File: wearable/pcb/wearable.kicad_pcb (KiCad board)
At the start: 4 copper layers, 28 x 39.2 mm, 83 parts, among them J1 USB_C_Receptacle_USB2.0, J2 Extension, J3 Extension, U1 BC833, U10 TCR3UFxxA, U11 TMP1075, U2 MCP73832-2-OT, U3 S-85S1A, U4 LIS2DE12, U5 APDS-9250, U6 MX25R8035FZxxx0, U7 PCF85063ATL, U8 DT1446-04V, U9 MAX30102, Y71 32.768kHz

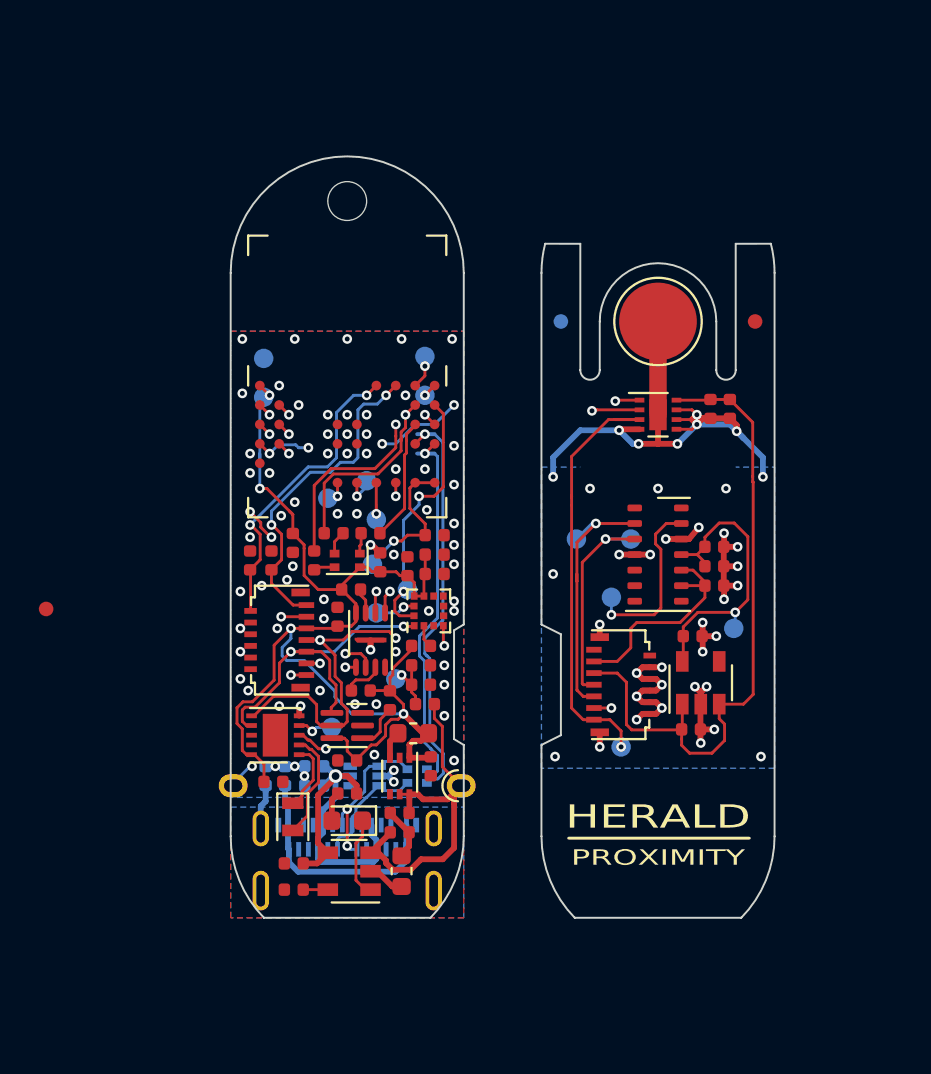
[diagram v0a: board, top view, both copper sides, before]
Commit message: The very first prototype, panelized.
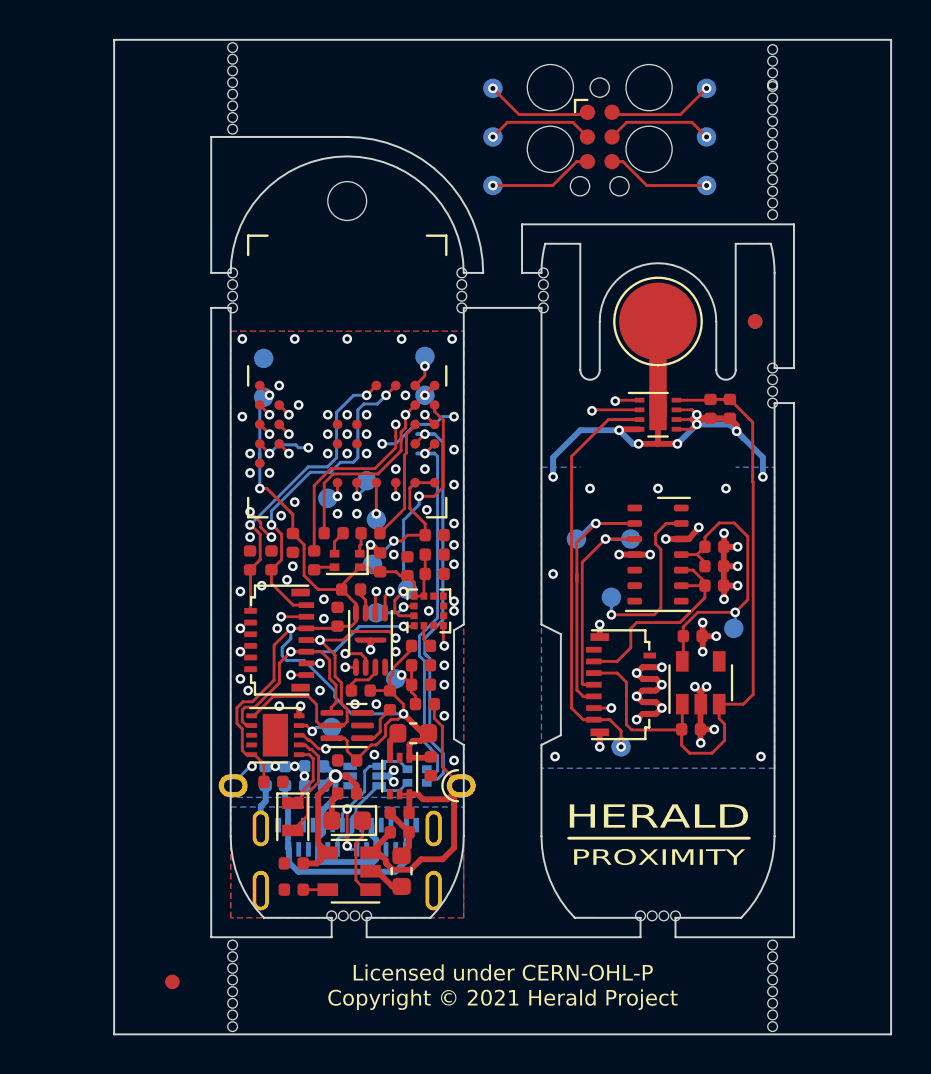
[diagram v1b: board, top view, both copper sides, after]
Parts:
- added J4: TagConnect, Connector:Tag-Connect_TC2030-IDC-FP_2x03_P1.27mm_Vertical, F.Cu at (163.0, 78.5)
- added REF**: MouseBites_4x0.5mm, Herald_Extras:MouseBites_4x0.5mm, F.Cu at (171.9, 74.9)
- added REF**: MouseBites_4x0.5mm, Herald_Extras:MouseBites_4x0.5mm, F.Cu at (166.0, 118.6)
- added REF**: MouseBites_4x0.5mm, Herald_Extras:MouseBites_4x0.5mm, F.Cu at (150.1, 118.6)
- added REF**: MouseBites_4x0.5mm, Herald_Extras:MouseBites_4x0.5mm, F.Cu at (144.1, 77.2)
- added REF**: MouseBites_4x0.5mm, Herald_Extras:MouseBites_4x0.5mm, F.Cu at (171.9, 121.0)
- added REF**: MouseBites_4x0.5mm, Herald_Extras:MouseBites_4x0.5mm, F.Cu at (171.9, 91.3)
- added REF**: MouseBites_4x0.5mm, Herald_Extras:MouseBites_4x0.5mm, F.Cu at (160.1, 86.4)
- added REF**: MouseBites_4x0.5mm, Herald_Extras:MouseBites_4x0.5mm, F.Cu at (155.9, 86.4)
- added REF**: MouseBites_4x0.5mm, Herald_Extras:MouseBites_4x0.5mm, F.Cu at (171.9, 76.8)
- added REF**: MouseBites_4x0.5mm, Herald_Extras:MouseBites_4x0.5mm, F.Cu at (171.9, 79.2)
- added REF**: MouseBites_4x0.5mm, Herald_Extras:MouseBites_4x0.5mm, F.Cu at (171.9, 81.6)
- added REF**: MouseBites_4x0.5mm, Herald_Extras:MouseBites_4x0.5mm, F.Cu at (171.9, 123.4)
- added REF**: MouseBites_4x0.5mm, Herald_Extras:MouseBites_4x0.5mm, F.Cu at (144.1, 123.4)
- added REF**: MouseBites_4x0.5mm, Herald_Extras:MouseBites_4x0.5mm, F.Cu at (144.1, 121.0)
- added REF**: MouseBites_4x0.5mm, Herald_Extras:MouseBites_4x0.5mm, F.Cu at (144.1, 86.4)
- added REF**: MouseBites_4x0.5mm, Herald_Extras:MouseBites_4x0.5mm, F.Cu at (144.1, 74.8)
- added TP401: TestPoint, TestPoint:TestPoint_Pad_D1.0mm, B.Cu at (157.5, 76.0)
- added TP402: TestPoint, TestPoint:TestPoint_Pad_D1.0mm, B.Cu at (168.5, 76.0)
- added TP403: TestPoint, TestPoint:TestPoint_Pad_D1.0mm, B.Cu at (157.5, 78.5)
- added TP404: TestPoint, TestPoint:TestPoint_Pad_D1.0mm, B.Cu at (168.5, 78.5)
- added TP405: TestPoint, TestPoint:TestPoint_Pad_D1.0mm, B.Cu at (157.5, 81.0)
- added TP406: TestPoint, TestPoint:TestPoint_Pad_D1.0mm, B.Cu at (168.5, 81.0)
- moved FID1 20.3 mm to (141.0, 122.0)
- moved FID4 10.0 mm to (171.0, 88.0)
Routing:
- net /Extension Board/TC_SWDCLK: track 0.00 -> 5.49 mm, vias 0 -> 1
- net /Extension Board/TC_RESET: track 0.00 -> 5.49 mm, vias 0 -> 1
- net /Extension Board/TC_VREF: track 0.00 -> 5.47 mm, vias 0 -> 1
- net /Extension Board/TC_SWDIO: track 0.00 -> 5.47 mm, vias 0 -> 1
- net /Extension Board/TC_SWO: track 0.00 -> 5.37 mm, vias 0 -> 1
- net /Extension Board/TC_GND: track 0.00 -> 5.37 mm, vias 0 -> 1
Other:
- board size 28 x 39.2 mm -> 40 x 51.2 mm
- board text added: "GND"
- board text added: "Licensed under CERN-OHL-P Copyright © 2021 Herald Project"
- board text added: "RST"
- board text added: "SWDCLK"
- board text added: "SWDIO"
- board text added: "SWO"
- board text added: "VREF"
- board text removed: "— NO PANEL MOUNTS ON THIS SIDE —"
